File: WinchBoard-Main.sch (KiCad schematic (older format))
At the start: 10 parts

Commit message: Checkpoint
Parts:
- removed P?: CONN_02X05, symbol CONN_02X05
- removed P?: CONN_01X06, symbol CONN_01X06
- removed P?: CONN_01X02, symbol CONN_01X02
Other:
- moved on the sheet: P?
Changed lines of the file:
@@
 $EndDescr
-$Comp
-L CONN_02X05 P?
-U 1 1 5B93FC94
-P 2450 2200
-F 0 "P?" H 2450 2500 50  0000 C CNN
-F 1 "CONN_02X05" H 2450 1900 50  0000 C CNN
-F 2 "" H 2450 1000 50  0000 C CNN
-F 3 "" H 2450 1000 50  0000 C CNN
-	1    2450 2200
-	1    0    0    -1
-$EndComp
 $Comp
 L CONN_02X07 P?
 U 1 1 5B93FCD7
-P 2450 3650
-F 0 "P?" H 2450 4050 50  0000 C CNN
-F 1 "CONN_02X07" V 2450 3650 50  0000 C CNN
-F 2 "" H 2450 2450 50  0000 C CNN
-F 3 "" H 2450 2450 50  0000 C CNN
-	1    2450 3650
+P 2250 1900
+F 0 "P?" H 2250 2300 50  0000 C CNN
+F 1 "CONN_02X07" V 2250 1900 50  0000 C CNN
+F 2 "" H 2250 700 50  0000 C CNN
+F 3 "" H 2250 700 50  0000 C CNN
+	1    2250 1900
 	1    0    0    -1
 $EndComp
@@
 L CONN_01X03 P?
 U 1 1 5B93FF1F
-P 4100 3450
-F 0 "P?" H 4100 3650 50  0000 C CNN
-F 1 "CONN_01X03" V 4200 3450 50  0000 C CNN
-F 2 "" H 4100 3450 50  0000 C CNN
-F 3 "" H 4100 3450 50  0000 C CNN
-	1    4100 3450
-	1    0    0    -1
-$EndComp
-$Comp
-L CONN_01X06 P?
-U 1 1 5B93FF8A
-P 4150 2050
-F 0 "P?" H 4150 2400 50  0000 C CNN
-F 1 "CONN_01X06" V 4250 2050 50  0000 C CNN
-F 2 "" H 4150 2050 50  0000 C CNN
-F 3 "" H 4150 2050 50  0000 C CNN
-	1    4150 2050
-	1    0    0    -1
-$EndComp
-$Comp
-L CONN_01X02 P?
-U 1 1 5B93FFB2
-P 4100 2700
-F 0 "P?" H 4100 2850 50  0000 C CNN
-F 1 "CONN_01X02" V 4200 2700 50  0000 C CNN
-F 2 "" H 4100 2700 50  0000 C CNN
-F 3 "" H 4100 2700 50  0000 C CNN
-	1    4100 2700
-	1    0    0    -1
+P 1500 1700
+F 0 "P?" H 1500 1900 50  0000 C CNN
+F 1 "CONN_01X03" V 1600 1700 50  0000 C CNN
+F 2 "" H 1500 1700 50  0000 C CNN
+F 3 "" H 1500 1700 50  0000 C CNN
+	1    1500 1700
+	-1   0    0    1
 $EndComp
 $Comp
@@
 	1    0    0    -1
 $EndComp
-Text GLabel 3750 1800 0    50   Input ~ 0
-Step
+$Comp
+L GNDD #PWR?
+U 1 1 5B941BC8
+P 2600 2400
+F 0 "#PWR?" H 2600 2150 50  0001 C CNN
+F 1 "GNDD" H 2600 2250 50  0000 C CNN
+F 2 "" H 2600 2400 50  0000 C CNN
+F 3 "" H 2600 2400 50  0000 C CNN
+	1    2600 2400
+	1    0    0    -1
+$EndComp
+$Comp
+L GNDA #PWR?
+U 1 1 5B941BF0
+P 1700 1200
+F 0 "#PWR?" H 1700 950 50  0001 C CNN
+F 1 "GNDA" H 1700 1050 50  0000 C CNN
+F 2 "" H 1700 1200 50  0000 C CNN
+F 3 "" H 1700 1200 50  0000 C CNN
+	1    1700 1200
+	1    0    0    -1
+$EndComp
 $EndSCHEMATC

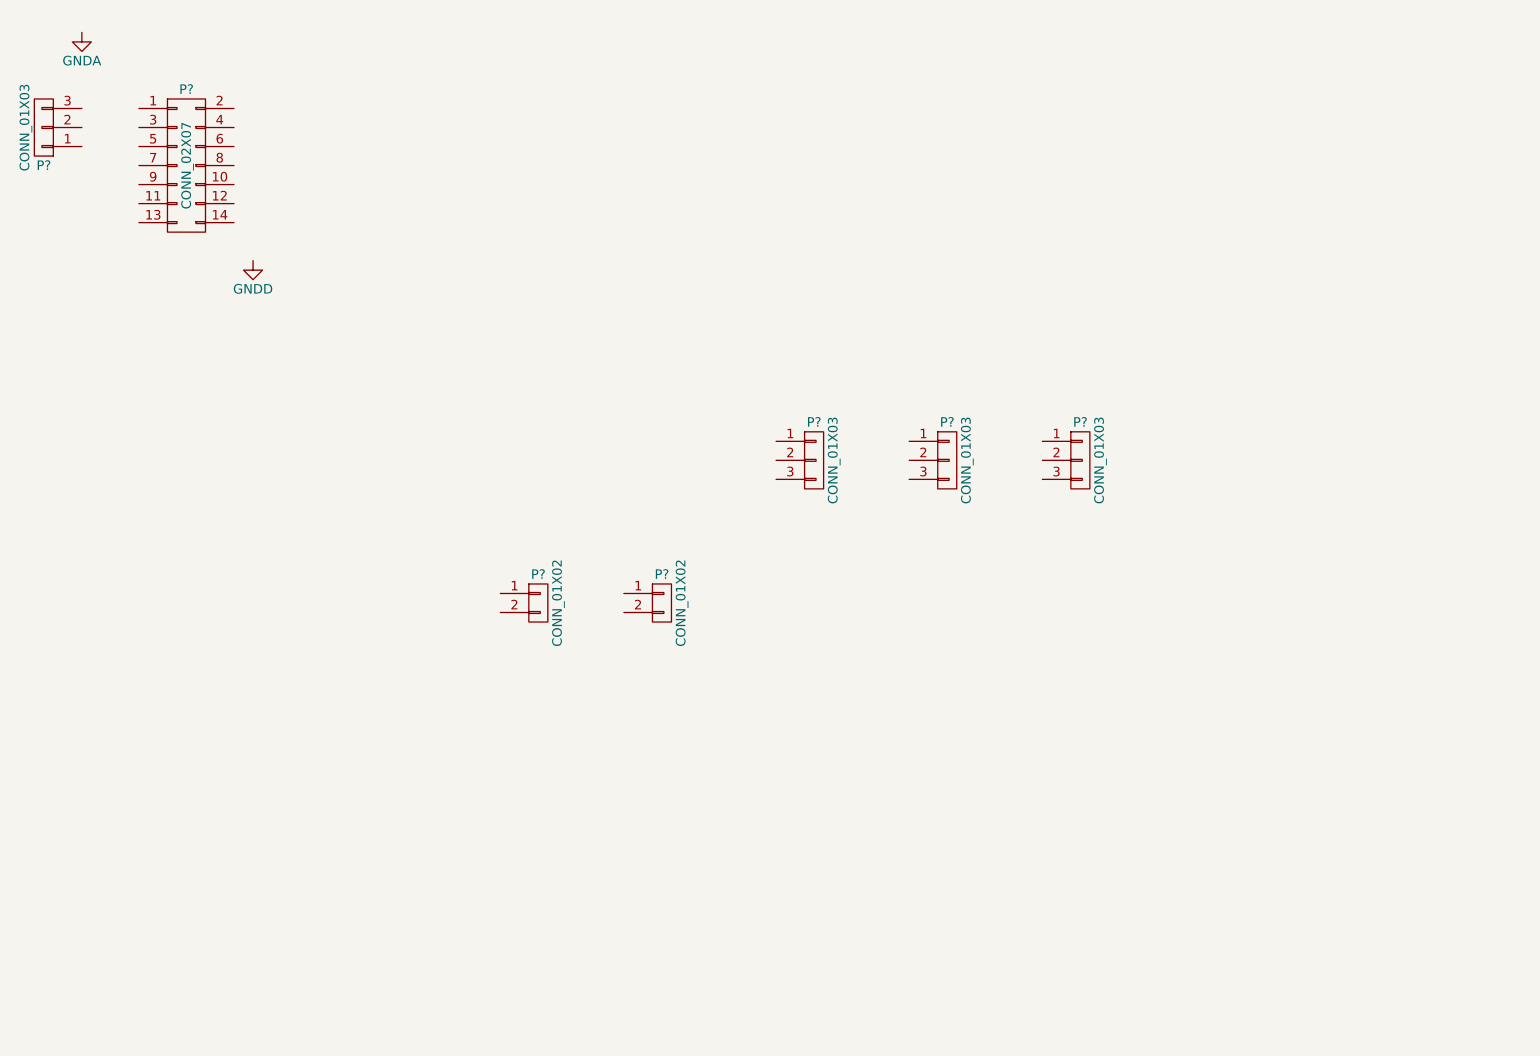
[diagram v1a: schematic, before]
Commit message: Added HDMI connector & libs, some component positioning, mounting holes, fiducials
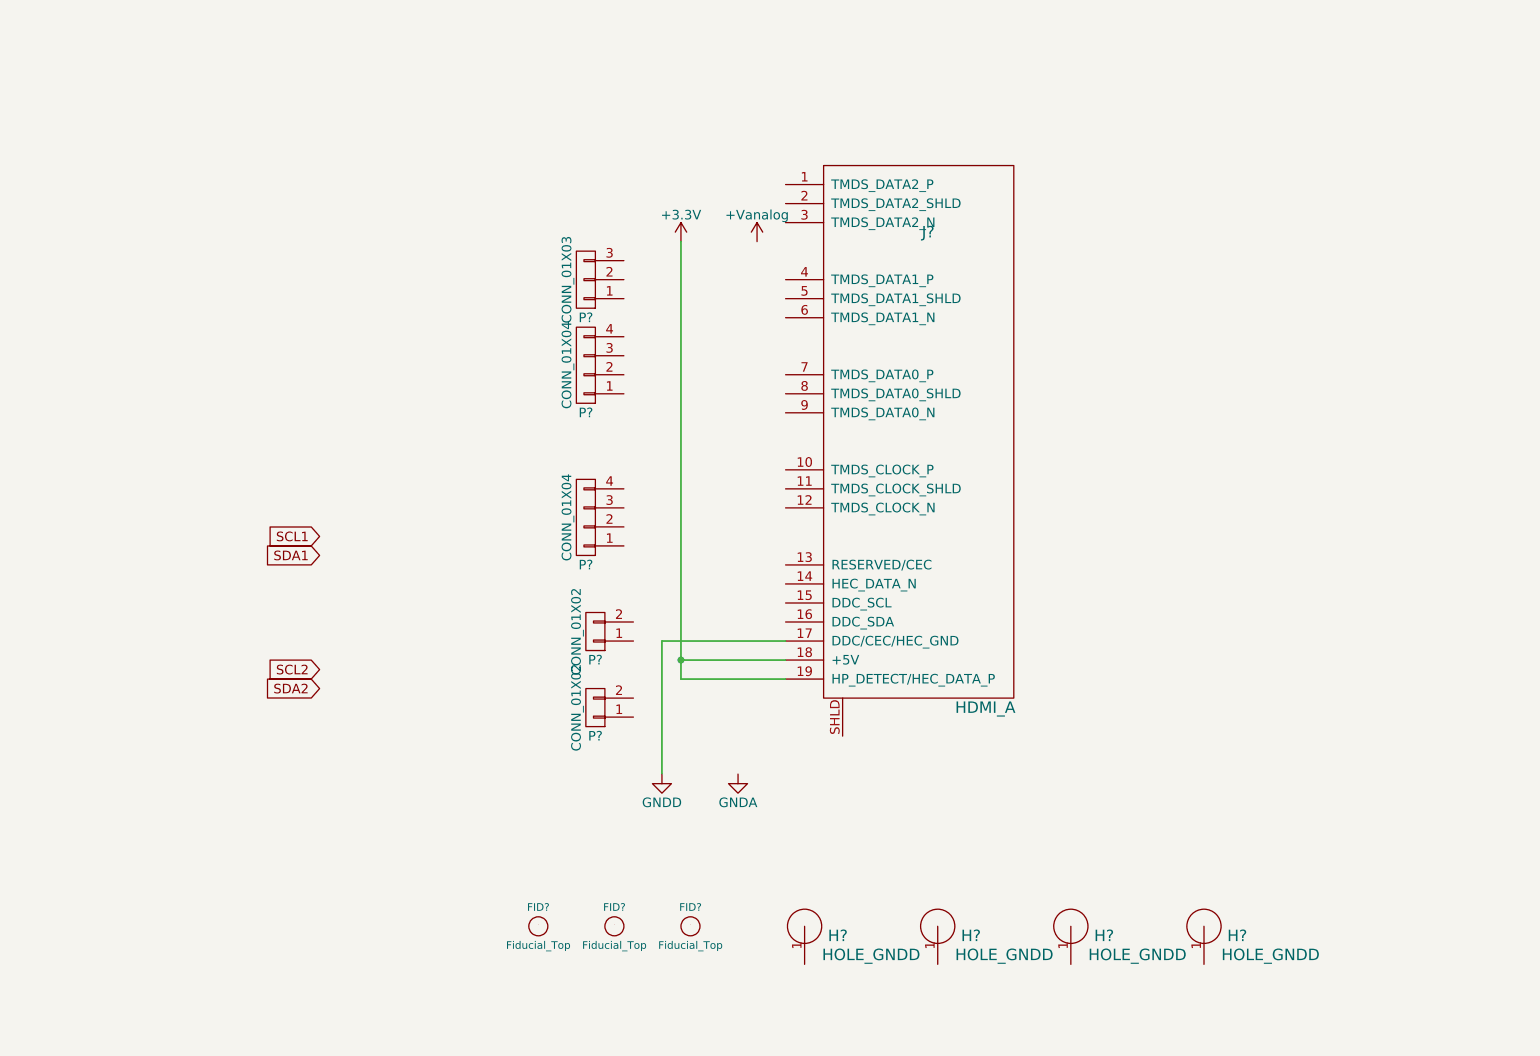
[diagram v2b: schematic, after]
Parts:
- removed P?: CONN_02X07, symbol CONN_02X07
- removed P? (x3): CONN_01X03, symbol CONN_01X03
- added FID? (x3): Fiducial_Top, symbol Fiducial_Top
- added H? (x4): HOLE_GNDD, symbol HOLE_GNDD
- added J?: HDMI_A, symbol HDMI_A
- added P? (x2): CONN_01X04, symbol CONN_01X04
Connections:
- net GNDD: now also J?.17 (DDC/CEC/HEC_GND)
- new net +3V3: J?.18 (+5V), J?.19 (HP_DETECT/HEC_DATA_P)
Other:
- moved on the sheet: P?
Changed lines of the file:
@@
 LIBS:_Connector
 LIBS:_Passive
+LIBS:hdmi
 LIBS:WinchBoard-cache
 EELAYER 25 0
@@
 $EndDescr
 $Comp
-L CONN_02X07 P?
-U 1 1 5B93FCD7
-P 2250 1900
-F 0 "P?" H 2250 2300 50  0000 C CNN
-F 1 "CONN_02X07" V 2250 1900 50  0000 C CNN
-F 2 "" H 2250 700 50  0000 C CNN
-F 3 "" H 2250 700 50  0000 C CNN
-	1    2250 1900
-	1    0    0    -1
-$EndComp
-$Comp
 L CONN_01X03 P?
 U 1 1 5B93FF1F
-P 1500 1700
-F 0 "P?" H 1500 1900 50  0000 C CNN
-F 1 "CONN_01X03" V 1600 1700 50  0000 C CNN
-F 2 "" H 1500 1700 50  0000 C CNN
-F 3 "" H 1500 1700 50  0000 C CNN
-	1    1500 1700
-	-1   0    0    1
-$EndComp
-$Comp
-L CONN_01X03 P?
-U 1 1 5B940075
-P 5550 3450
-F 0 "P?" H 5550 3650 50  0000 C CNN
-F 1 "CONN_01X03" V 5650 3450 50  0000 C CNN
-F 2 "" H 5550 3450 50  0000 C CNN
-F 3 "" H 5550 3450 50  0000 C CNN
-	1    5550 3450
-	1    0    0    -1
-$EndComp
-$Comp
-L CONN_01X03 P?
-U 1 1 5B9400BD
-P 6250 3450
-F 0 "P?" H 6250 3650 50  0000 C CNN
-F 1 "CONN_01X03" V 6350 3450 50  0000 C CNN
-F 2 "" H 6250 3450 50  0000 C CNN
-F 3 "" H 6250 3450 50  0000 C CNN
-	1    6250 3450
-	1    0    0    -1
-$EndComp
-$Comp
-L CONN_01X03 P?
-U 1 1 5B9400E2
-P 6950 3450
-F 0 "P?" H 6950 3650 50  0000 C CNN
-F 1 "CONN_01X03" V 7050 3450 50  0000 C CNN
-F 2 "" H 6950 3450 50  0000 C CNN
-F 3 "" H 6950 3450 50  0000 C CNN
-	1    6950 3450
-	1    0    0    -1
+P 4350 2500
+F 0 "P?" H 4350 2700 50  0000 C CNN
+F 1 "CONN_01X03" V 4450 2500 50  0000 C CNN
+F 2 "" H 4350 2500 50  0000 C CNN
+F 3 "" H 4350 2500 50  0000 C CNN
+	1    4350 2500
+	-1   0    0    1
 $EndComp
 $Comp
 L CONN_01X02 P?
 U 1 1 5B940141
-P 4100 4200
-F 0 "P?" H 4100 4350 50  0000 C CNN
-F 1 "CONN_01X02" V 4200 4200 50  0000 C CNN
-F 2 "" H 4100 4200 50  0000 C CNN
-F 3 "" H 4100 4200 50  0000 C CNN
-	1    4100 4200
-	1    0    0    -1
+P 4400 4750
+F 0 "P?" H 4400 4900 50  0000 C CNN
+F 1 "CONN_01X02" V 4500 4750 50  0000 C CNN
+F 2 "" H 4400 4750 50  0000 C CNN
+F 3 "" H 4400 4750 50  0000 C CNN
+	1    4400 4750
+	-1   0    0    1
 $EndComp
 $Comp
 L CONN_01X02 P?
 U 1 1 5B940168
-P 4750 4200
-F 0 "P?" H 4750 4350 50  0000 C CNN
-F 1 "CONN_01X02" V 4850 4200 50  0000 C CNN
-F 2 "" H 4750 4200 50  0000 C CNN
-F 3 "" H 4750 4200 50  0000 C CNN
-	1    4750 4200
-	1    0    0    -1
+P 4400 4350
+F 0 "P?" H 4400 4500 50  0000 C CNN
+F 1 "CONN_01X02" V 4500 4350 50  0000 C CNN
+F 2 "" H 4400 4350 50  0000 C CNN
+F 3 "" H 4400 4350 50  0000 C CNN
+	1    4400 4350
+	-1   0    0    1
 $EndComp
 $Comp
 L GNDD #PWR?
 U 1 1 5B941BC8
-P 2600 2400
-F 0 "#PWR?" H 2600 2150 50  0001 C CNN
-F 1 "GNDD" H 2600 2250 50  0000 C CNN
-F 2 "" H 2600 2400 50  0000 C CNN
-F 3 "" H 2600 2400 50  0000 C CNN
-	1    2600 2400
+P 4750 5100
+F 0 "#PWR?" H 4750 4850 50  0001 C CNN
+F 1 "GNDD" H 4750 4950 50  0000 C CNN
+F 2 "" H 4750 5100 50  0000 C CNN
+F 3 "" H 4750 5100 50  0000 C CNN
+	1    4750 5100
 	1    0    0    -1
 $EndComp
@@
 L GNDA #PWR?
 U 1 1 5B941BF0
-P 1700 1200
-F 0 "#PWR?" H 1700 950 50  0001 C CNN
-F 1 "GNDA" H 1700 1050 50  0000 C CNN
-F 2 "" H 1700 1200 50  0000 C CNN
-F 3 "" H 1700 1200 50  0000 C CNN
-	1    1700 1200
-	1    0    0    -1
-$EndComp
+P 5150 5100
+F 0 "#PWR?" H 5150 4850 50  0001 C CNN
+F 1 "GNDA" H 5150 4950 50  0000 C CNN
+F 2 "" H 5150 5100 50  0000 C CNN
+F 3 "" H 5150 5100 50  0000 C CNN
+	1    5150 5100
+	1    0    0    -1
+$EndComp
+$Comp
+L HDMI_A J?
+U 1 1 5B94EAB0
+P 6100 3500
+F 0 "J?" H 6150 4750 60  0000 C CNN
+F 1 "HDMI_A" H 6450 2250 60  0000 C CNN
+F 2 "" H 5600 3000 60  0000 C CNN
+F 3 "" H 5600 3000 60  0000 C CNN
+	1    6100 3500
+	1    0    0    -1
+$EndComp
+$Comp
+L CONN_01X04 P?
+U 1 1 5B94F60A
+P 4350 2950
+F 0 "P?" H 4350 3200 50  0000 C CNN
+F 1 "CONN_01X04" V 4450 2950 50  0000 C CNN
+F 2 "" H 4350 2950 50  0000 C CNN
+F 3 "" H 4350 2950 50  0000 C CNN
+	1    4350 2950
+	-1   0    0    1
+$EndComp
+$Comp
+L CONN_01X04 P?
+U 1 1 5B94F646
+P 4350 3750
+F 0 "P?" H 4350 4000 50  0000 C CNN
+F 1 "CONN_01X04" V 4450 3750 50  0000 C CNN
+F 2 "" H 4350 3750 50  0000 C CNN
+F 3 "" H 4350 3750 50  0000 C CNN
+	1    4350 3750
+	-1   0    0    1
+$EndComp
+Text GLabel 2950 3850 0    50   Input ~ 0
+SCL1
+Text GLabel 2950 3950 0    50   Input ~ 0
+SDA1
+$Comp
+L +3.3V #PWR?
+U 1 1 5B94F6A3
+P 4850 2300
+F 0 "#PWR?" H 4850 2150 50  0001 C CNN
+F 1 "+3.3V" H 4850 2440 50  0000 C CNN
+F 2 "" H 4850 2300 50  0000 C CNN
+F 3 "" H 4850 2300 50  0000 C CNN
+	1    4850 2300
+	1    0    0    -1
+$EndComp
+$Comp
+L +Vanalog #PWR?
+U 1 1 5B94F6C9
+P 5250 2300
+F 0 "#PWR?" H 5250 2150 50  0001 C CNN
+F 1 "+Vanalog" H 5250 2440 50  0000 C CNN
+F 2 "" H 5250 2300 50  0000 C CNN
+F 3 "" H 5250 2300 50  0000 C CNN
+	1    5250 2300
+	1    0    0    -1
+$EndComp
+Text GLabel 2950 4550 0    50   Input ~ 0
+SCL2
+Text GLabel 2950 4650 0    50   Input ~ 0
+SDA2
+Wire Wire Line
+	5400 4400 4750 4400
+Wire Wire Line
+	4750 4400 4750 5100
+Wire Wire Line
+	5400 4500 4850 4500
+Wire Wire Line
+	4850 2300 4850 4600
+Wire Wire Line
+	4850 4600 5400 4600
+Connection ~ 4850 4500
+$Comp
+L Fiducial_Top FID?
+U 1 1 5B94FE95
+P 4100 5900
+F 0 "FID?" H 4100 6000 40  0000 C CNN
+F 1 "Fiducial_Top" H 4100 5800 40  0000 C CNN
+F 2 "" H 4100 5900 150 0000 C CNN
+F 3 "" H 4100 5900 150 0000 C CNN
+	1    4100 5900
+	1    0    0    -1
+$EndComp
+$Comp
+L Fiducial_Top FID?
+U 1 1 5B94FF3C
+P 4500 5900
+F 0 "FID?" H 4500 6000 40  0000 C CNN
+F 1 "Fiducial_Top" H 4500 5800 40  0000 C CNN
+F 2 "" H 4500 5900 150 0000 C CNN
+F 3 "" H 4500 5900 150 0000 C CNN
+	1    4500 5900
+	1    0    0    -1
+$EndComp
+$Comp
+L Fiducial_Top FID?
+U 1 1 5B94FF61
+P 4900 5900
+F 0 "FID?" H 4900 6000 40  0000 C CNN
+F 1 "Fiducial_Top" H 4900 5800 40  0000 C CNN
+F 2 "" H 4900 5900 150 0000 C CNN
+F 3 "" H 4900 5900 150 0000 C CNN
+	1    4900 5900
+	1    0    0    -1
+$EndComp
+$Comp
+L HOLE_GNDD H?
+U 1 1 5B94FFB7
+P 5500 5900
+F 0 "H?" H 5675 5850 60  0000 C CNN
+F 1 "HOLE_GNDD" H 5850 5750 60  0000 C CNN
+F 2 "" H 5475 5675 60  0000 C CNN
+F 3 "" H 5475 5675 60  0000 C CNN
+	1    5500 5900
+	1    0    0    -1
+$EndComp
+$Comp
+L HOLE_GNDD H?
+U 1 1 5B950003
+P 6200 5900
+F 0 "H?" H 6375 5850 60  0000 C CNN
+F 1 "HOLE_GNDD" H 6550 5750 60  0000 C CNN
+F 2 "" H 6175 5675 60  0000 C CNN
+F 3 "" H 6175 5675 60  0000 C CNN
+	1    6200 5900
+	1    0    0    -1
+$EndComp
+$Comp
+L HOLE_GNDD H?
+U 1 1 5B950035
+P 6900 5900
+F 0 "H?" H 7075 5850 60  0000 C CNN
+F 1 "HOLE_GNDD" H 7250 5750 60  0000 C CNN
+F 2 "" H 6875 5675 60  0000 C CNN
+F 3 "" H 6875 5675 60  0000 C CNN
+	1    6900 5900
+	1    0    0    -1
+$EndComp
+$Comp
+L HOLE_GNDD H?
+U 1 1 5B950064
+P 7600 5900
+F 0 "H?" H 7775 5850 60  0000 C CNN
+F 1 "HOLE_GNDD" H 7950 5750 60  0000 C CNN
+F 2 "" H 7575 5675 60  0000 C CNN
+F 3 "" H 7575 5675 60  0000 C CNN
+	1    7600 5900
+	1    0    0    -1
+$EndComp

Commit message: First complete schematic
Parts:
- removed J?: HDMI_A, symbol HDMI_A
- added J1: HDMI_A, _Connector:FCI_10029449-11[13]RLF, symbol HDMI_A
- added P1: CONN_01X04, _Connector:0.100_1x4_small, symbol CONN_01X04
- added P6: CONN_01X02, _Connector:0.100_1x2_small, symbol CONN_01X02
- added TT1: SCL1, _Connector:Test_Point_SMD_0.040_Top, symbol TP_Top
- added TT10: +Vanalog, _Connector:Test_Point_SMD_0.040_Top, symbol TP_Top
- added TT2: SDA1, _Connector:Test_Point_SMD_0.040_Top, symbol TP_Top
- added TT3: SCL2, _Connector:Test_Point_SMD_0.040_Top, symbol TP_Top
- added TT4: SDA2, _Connector:Test_Point_SMD_0.040_Top, symbol TP_Top
- added TT5: SCL3, _Connector:Test_Point_SMD_0.040_Top, symbol TP_Top
- added TT6: SDA3, _Connector:Test_Point_SMD_0.040_Top, symbol TP_Top
- added TT7: DI1, _Connector:Test_Point_SMD_0.040_Top, symbol TP_Top
- added TT8: DI2, _Connector:Test_Point_SMD_0.040_Top, symbol TP_Top
- added TT9: +3.3v, _Connector:Test_Point_SMD_0.040_Top, symbol TP_Top
- FID1, FID2, FID3: renamed from FID?; footprint (none) -> _Connector:Fiducial_0.040_Top
- H1, H2, H3, H4: renamed from H?; footprint (none) -> _Connector:MountingHole_3.2mm_M3
- P2, P3: renamed from P?; footprint (none) -> _Connector:0.100_1x4_small
- P4, P5: renamed from P?; footprint (none) -> _Connector:0.100_1x2_small
- P7: renamed from P?; footprint (none) -> _Connector:0.100_1x3_small
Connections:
- net +3V3: now also P2.4 (P4), P3.4 (P4), J1.18 (+5V), J1.19 (HP_DETECT/HEC_DATA_P), P1.4 (P4), TT9.1 (TP)
- net +Vanalog: now also P7.3 (P3), J1.1 (TMDS_DATA2_P), TT10.1 (TP)
- net GNDA: now also P7.2 (P2), J1.2 (TMDS_DATA2_SHLD)
- net GNDD: now also H1.1 (GND), H2.1 (GND), H3.1 (GND), H4.1 (GND), P2.3 (P3), P3.3 (P3), P4.2 (P2), P5.2 (P2), J1.11 (TMDS_CLOCK_SHLD), J1.16 (DDC_SDA), J1.17 (DDC/CEC/HEC_GND), J1.5 (TMDS_DATA1_SHLD), J1.8 (TMDS_DATA0_SHLD), J1.SHLD, P1.3 (P3), P6.2 (P2)
- net SCL1: now also J1.10 (TMDS_CLOCK_P), P1.1 (P1), TT1.1 (TP)
- net SCL2: now also P2.1 (P1), J1.7 (TMDS_DATA0_P), TT3.1 (TP)
- net SDA1: now also J1.12 (TMDS_CLOCK_N), P1.2 (P2), TT2.1 (TP)
- net SDA2: now also P2.2 (P2), J1.9 (TMDS_DATA0_N), TT4.1 (TP)
- net Aout: now reaches P7.1 (P1)
- net Aout: now also J1.3 (TMDS_DATA2_N)
- net DI2: now reaches P5.1 (P1)
- net DI2: now also J1.15 (DDC_SCL), TT8.1 (TP)
- net DI1: now reaches P4.1 (P1)
- net DI1: now also J1.14 (HEC_DATA_N), TT7.1 (TP)
- net SCL3: now reaches P3.1 (P1)
- net SCL3: now also J1.4 (TMDS_DATA1_P), TT5.1 (TP)
- net SDA3: now reaches P3.2 (P2)
- net SDA3: now also J1.6 (TMDS_DATA1_N), TT6.1 (TP)
- new net DO: J1.13 (RESERVED/CEC), P6.1 (P1)
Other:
- note added: "Digital Input 1"
- note added: "Digital Input 2"
- note added: "Digital Output"
- note added: "Group A Twisted Pair"
- note added: "Group B Twisted Pair"
- note added: "Group C Twisted Pair"
- note added: "Group D Twisted Pair"
- note added: "I2C Channel 1"
- note added: "I2C Channel 2"
- note added: "I2C Channel 3"
- note added: "Load Cell"
- note added: "Note: There are no I2C termination resistors on this board.\nIt is assumd that these are on the other end of the line."
- moved on the sheet: FID1, FID2, FID3, H1, H2, H3, H4, P2, P3, P4, P5, P7

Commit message: Checkpoint
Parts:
- added TT10: Aout, _Connector:Test_Point_SMD_0.040_Top, symbol TP_Top
- P1, P2, P3: footprint _Connector:0.100_1x4_small -> Connectors_Molex:Molex_KK-6410-04_04x2.54mm_Straight
- P4, P5, P6: footprint _Connector:0.100_1x2_small -> Connectors_Molex:Molex_KK-6410-02_02x2.54mm_Straight
- renumbered TT10 to TT11
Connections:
- net Aout: now also TT10.1 (TP)
- net GNDD: no longer H1.1 (GND), H2.1 (GND), H3.1 (GND), H4.1 (GND)
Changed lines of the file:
@@
 F 0 "P5" H 5400 4650 50  0000 C CNN
 F 1 "CONN_01X02" V 5500 4500 50  0000 C CNN
-F 2 "_Connector:0.100_1x2_small" H 5400 4500 50  0001 C CNN
+F 2 "Connectors_Molex:Molex_KK-6410-02_02x2.54mm_Straight" H 5400 4500 50  0001 C CNN
 F 3 "" H 5400 4500 50  0000 C CNN
 	1    5400 4500
@@
 F 0 "P3" H 4650 2900 50  0000 C CNN
 F 1 "CONN_01X04" V 4750 2650 50  0000 C CNN
-F 2 "_Connector:0.100_1x4_small" H 4650 2650 50  0001 C CNN
+F 2 "Connectors_Molex:Molex_KK-6410-04_04x2.54mm_Straight" H 4650 2650 50  0001 C CNN
 F 3 "" H 4650 2650 50  0000 C CNN
 	1    4650 2650
@@
 F 0 "P2" H 3650 3400 50  0000 C CNN
 F 1 "CONN_01X04" V 3750 3150 50  0000 C CNN
-F 2 "_Connector:0.100_1x4_small" H 3650 3150 50  0001 C CNN
+F 2 "Connectors_Molex:Molex_KK-6410-04_04x2.54mm_Straight" H 3650 3150 50  0001 C CNN
 F 3 "" H 3650 3150 50  0000 C CNN
 	1    3650 3150
@@
 F 0 "P1" H 2750 3900 50  0000 C CNN
 F 1 "CONN_01X04" V 2850 3650 50  0000 C CNN
-F 2 "_Connector:0.100_1x4_small" H 2750 3650 50  0001 C CNN
+F 2 "Connectors_Molex:Molex_KK-6410-04_04x2.54mm_Straight" H 2750 3650 50  0001 C CNN
 F 3 "" H 2750 3650 50  0000 C CNN
 	1    2750 3650
@@
 F 0 "P4" H 5150 4300 50  0000 C CNN
 F 1 "CONN_01X02" V 5250 4150 50  0000 C CNN
-F 2 "_Connector:0.100_1x2_small" H 5150 4150 50  0001 C CNN
+F 2 "Connectors_Molex:Molex_KK-6410-02_02x2.54mm_Straight" H 5150 4150 50  0001 C CNN
 F 3 "" H 5150 4150 50  0000 C CNN
 	1    5150 4150
@@
 Connection ~ 6200 4400
 $Comp
-L TP_Top TT10
+L TP_Top TT11
 U 1 1 5B952A2E
 P 6950 1450
-F 0 "TT10" H 7000 1480 35  0000 C CNN
+F 0 "TT11" H 7000 1480 35  0000 C CNN
 F 1 "+Vanalog" H 6960 1580 50  0000 C CNN
 F 2 "_Connector:Test_Point_SMD_0.040_Top" H 6950 1500 50  0001 C CNN
@@
 F 0 "P6" H 5600 5050 50  0000 C CNN
 F 1 "CONN_01X02" V 5700 4900 50  0000 C CNN
-F 2 "_Connector:0.100_1x2_small" H 5600 4900 50  0001 C CNN
+F 2 "Connectors_Molex:Molex_KK-6410-02_02x2.54mm_Straight" H 5600 4900 50  0001 C CNN
 F 3 "" H 5600 4900 50  0000 C CNN
 	1    5600 4900
@@
 Text Label 6550 4000 0    40   ~ 0
 DO
-$Comp
-L GNDD #PWR05
-U 1 1 5B955CD6
-P 4800 6300
-F 0 "#PWR05" H 4800 6050 50  0001 C CNN
-F 1 "GNDD" H 4800 6150 50  0000 C CNN
-F 2 "" H 4800 6300 50  0000 C CNN
-F 3 "" H 4800 6300 50  0000 C CNN
-	1    4800 6300
-	1    0    0    -1
-$EndComp
-Wire Wire Line
-	4800 6100 4800 6300
-Wire Wire Line
-	4800 6200 6900 6200
-Wire Wire Line
-	6900 6200 6900 6100
-Connection ~ 4800 6200
-Wire Wire Line
-	6200 6100 6200 6200
-Connection ~ 6200 6200
-Wire Wire Line
-	5500 6100 5500 6200
-Connection ~ 5500 6200
-Text Label 6500 2200 0    40   ~ 0
+Text Label 6600 2200 0    40   ~ 0
 Aout
 Text Notes 5500 2050 0    60   ~ 0
@@
 Text Notes 8100 3600 0    60   ~ 0
 Group D Twisted Pair
+$Comp
+L TP_Top TT10
+U 1 1 5B958039
+P 6550 1950
+F 0 "TT10" H 6600 1980 35  0000 C CNN
+F 1 "Aout" H 6560 2080 50  0000 C CNN
+F 2 "_Connector:Test_Point_SMD_0.040_Top" H 6550 2000 50  0001 C CNN
+F 3 "" H 6550 2000 50  0000 C CNN
+	1    6550 1950
+	1    0    0    -1
+$EndComp
+Wire Wire Line
+	6550 1950 6550 2200
+Connection ~ 6550 2200
 $EndSCHEMATC
